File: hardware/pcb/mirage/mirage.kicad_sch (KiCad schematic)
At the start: 4 parts, among them U103 Adafruit ST7735R, U2 ESP32-S3-WROOM-1-N8

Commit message: feat: temporary pcb/schematic work
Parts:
- added C16, C17, C18, C19: 100 nf, Capacitor_SMD:C_0402_1005Metric, symbol Device:C
- added R10, R7, R8, R9: 100K, Resistor_SMD:R_0402_1005Metric, symbol Device:R
- added SW1: UP, Button_Switch_THT:SW_PUSH_6mm, symbol Switch:SW_Push
- added SW2: DOWN, Button_Switch_THT:SW_PUSH_6mm, symbol Switch:SW_Push
- added SW3: LEFT, Button_Switch_THT:SW_PUSH_6mm, symbol Switch:SW_Push
- added SW4: RIGHT, Button_Switch_THT:SW_PUSH_6mm, symbol Switch:SW_Push
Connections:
- net +3V3: now also R10.2, R7.2, R8.2, R9.2
- net GND: now also C16.2, C17.2, C18.2, C19.2, SW1.1, SW2.1, SW3.1, SW4.1
- net TFT_D/C: now also U2.33 (IO40)
- new net SW_DOWN: C17.1, R8.1, SW2.2
- new net SW_LEFT: C18.1, R9.1, SW3.2
- new net SW_RIGHT: C19.1, R10.1, SW4.2
- new net SW_UP: C16.1, R7.1, SW1.2
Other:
- note added: "I/O BUTTONS"
- note added: "I/O: On Button USB-c charger headphone jack 5 buttons bluetooth / wifi"

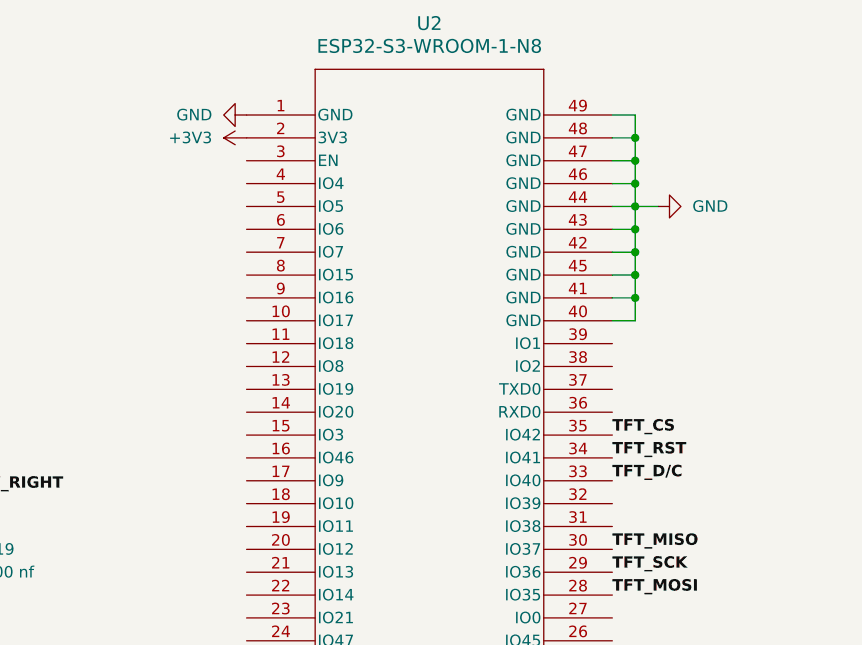
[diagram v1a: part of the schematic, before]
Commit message: fix: changed ST7735 pins to ESP32
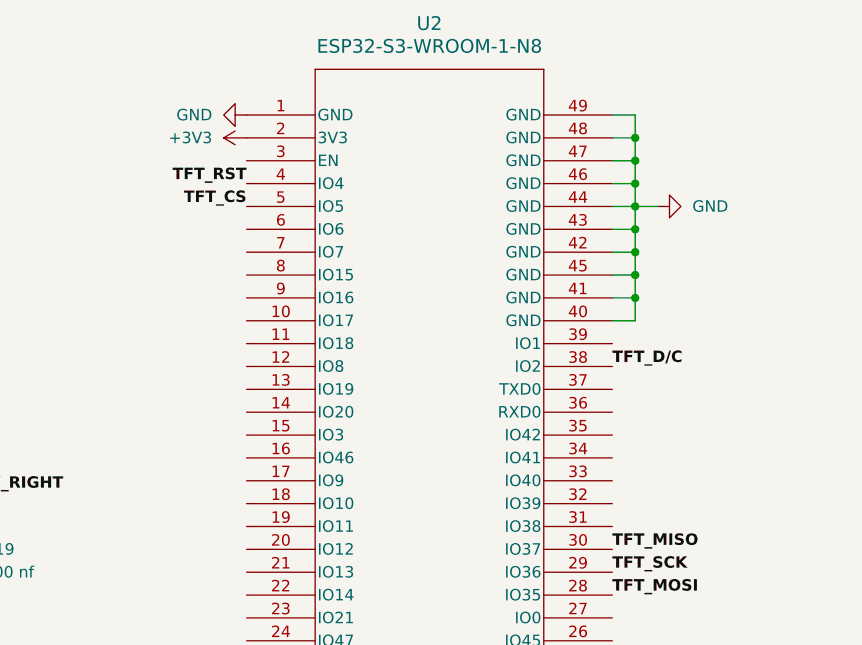
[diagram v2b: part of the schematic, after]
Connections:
- net TFT_CS: now also U2.5 (IO5); no longer U2.35 (IO42)
- net TFT_D/C: now also U2.38 (IO2); no longer U2.33 (IO40)
- net TFT_RST: now also U2.4 (IO4); no longer U2.34 (IO41)
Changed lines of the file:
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@@
     (effects (font (size 1.27 1.27) bold) (justify left bottom))
   )
-  (label "TFT_CS" (at 172.72 80.01 0) (fields_autoplaced)
-    (effects (font (size 1.27 1.27) bold) (justify left bottom))
+  (label "TFT_CS" (at 132.08 54.61 180) (fields_autoplaced)
+    (effects (font (size 1.27 1.27) bold) (justify right bottom))
   )
   (label "SW_LEFT" (at 78.74 86.36 0) (fields_autoplaced)
@@
     (effects (font (size 1.27 1.27) bold) (justify left bottom))
   )
+  (label "TFT_RST" (at 132.08 52.07 180) (fields_autoplaced)
+    (effects (font (size 1.27 1.27) bold) (justify right bottom))
+  )
   (label "TFT_D{slash}C" (at 21.59 50.8 180) (fields_autoplaced)
     (effects (font (size 1.27 1.27) bold) (justify right bottom))
@@
     (effects (font (size 1.27 1.27) bold) (justify left bottom))
   )
-  (label "TFT_D{slash}C" (at 172.72 85.09 0) (fields_autoplaced)
+  (label "TFT_D{slash}C" (at 172.72 72.39 0) (fields_autoplaced)
     (effects (font (size 1.27 1.27) bold) (justify left bottom))
   )
-  (label "TFT_RST" (at 172.72 82.55 0) (fields_autoplaced)
-    (effects (font (size 1.27 1.27) bold) (justify left bottom))
-  )

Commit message: feat: added footprints, schematics, and models
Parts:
- added IC1: TLV5618AIP, footprints:ti_TLV5618AIP, symbol ti_TLV5618AIP:TLV5618AIP
- added IC2: LM4041CILPR, footprints:ti_LM4041CILPR, symbol ti_LM4041CILPR:LM4041CILPR
- added J1: SJ1-3525N, footprints:PJ-307, symbol SJ1-3525N:SJ1-3525N
- added R1: 47k, symbol Device:R
- added R2: 10k, symbol Device:R
- added R3: 2k, symbol Device:R
- C102: footprint Capacitor_THT:C_Axial_L5.1mm_D3.1mm_P15.00mm_Horizontal -> Capacitor_SMD:C_0402_1005Metric
- C104: footprint Capacitor_THT:CP_Axial_L10.0mm_D4.5mm_P15.00mm_Horizontal -> Capacitor_SMD:C_0402_1005Metric
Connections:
- net GND: now also IC1.3 (~{CS}), IC1.5 (AGND), IC2.3, R2.1
- new net: IC2.1, R1.1, R2.2
- new net +3.3V: IC1.8 (VDD), R3.2
- new net DAC_FS: IC1.4 (OUTA)
- new net DAC_MOSI: IC1.1 (DIN)
- new net DAC_OUT: IC1.7 (OUTB)
- new net DAC_SCK: IC1.2 (SCLK)
- new net V_REF: IC1.6 (REF), IC2.2, R1.2, R3.1
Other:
- moved on the sheet: U2
